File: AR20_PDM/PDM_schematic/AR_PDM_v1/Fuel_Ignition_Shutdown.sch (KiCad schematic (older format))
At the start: 18 parts, among them K1 DIPxx-1Cxx-51x, K2 DIPxx-1Cxx-51x, Q18 N_FET, Q8 N_FET, Q9 N_FET, U2 INA233, U3 INA233

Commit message: Alpha version DONE! - Gerber files generated
- Tweeked
- checked and re cheked
- added all missing components
- Created a really nice silkscreen
- Ready To Test
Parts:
- K1, K2: footprint AR_PDM_v1:Relay -> AR_PDM_v1:Relay_wo_silkscreen
- renumbered C_bypass1 to C44, C_bypass2 to C45, D5 to D30, D6 to D31, Q18 to Q16, Q8 to Q17, Q9 to Q18, R_Shunt1 to R94, R_s13 to R95, R1 to R96, R_Shunt2 to R97, R2 to R98, U2 to U29, U3 to U30

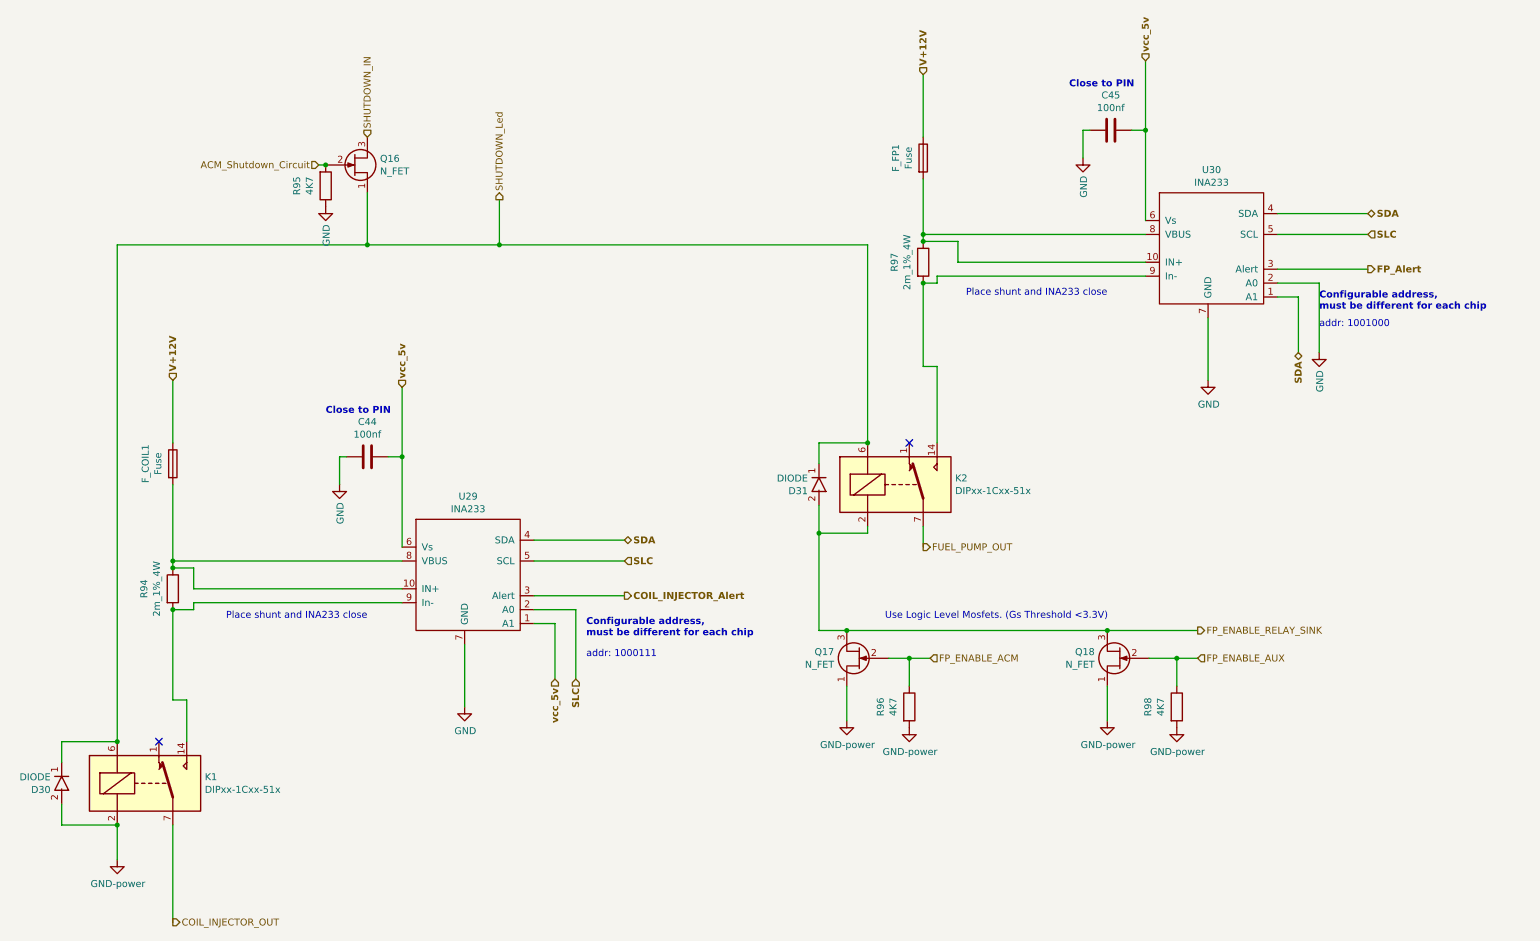
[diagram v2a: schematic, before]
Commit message: Fixed wrong resistors, mos sense. Gerber files updated
- removed all R_is_protection resistors on each mosfet line
- added one R_is_protection resistors to mos_sense_all
ps, mux N-fets, does not need overvoltage protection. 60 volt tolerant.
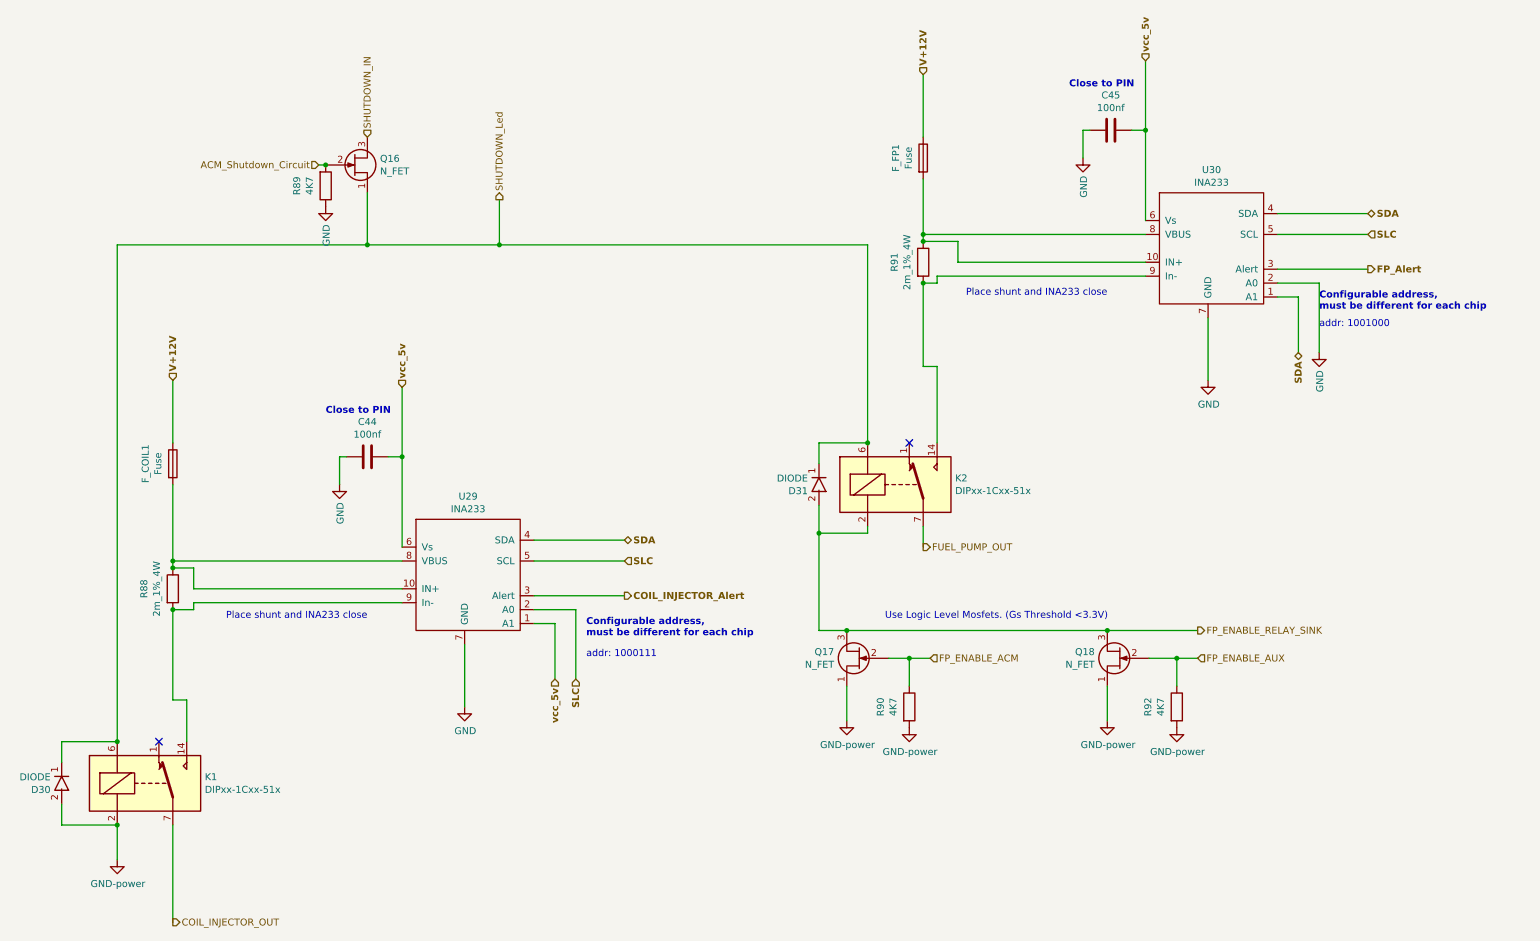
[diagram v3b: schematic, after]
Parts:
- renumbered R94 to R88, R95 to R89, R96 to R90, R97 to R91, R98 to R92
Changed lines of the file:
@@
 P 9175 5550
 AR Path="/5DA89415/5DDB5A5B" Ref="R?"  Part="1"
-AR Path="/5DA8920B/5DDB5A5B" Ref="R98"  Part="1"
-F 0 "R98" V 8968 5550 50  0000 C CNN
+AR Path="/5DA8920B/5DDB5A5B" Ref="R92"  Part="1"
+F 0 "R92" V 8968 5550 50  0000 C CNN
 F 1 "4K7" V 9059 5550 50  0000 C CNN
 F 2 "Resistor_SMD:R_0603_1608Metric" V 9105 5550 50  0001 C CNN
@@
 P 7250 5550
 AR Path="/5DA89415/5DDC298C" Ref="R?"  Part="1"
-AR Path="/5DA8920B/5DDC298C" Ref="R96"  Part="1"
-F 0 "R96" V 7043 5550 50  0000 C CNN
+AR Path="/5DA8920B/5DDC298C" Ref="R90"  Part="1"
+F 0 "R90" V 7043 5550 50  0000 C CNN
 F 1 "4K7" V 7134 5550 50  0000 C CNN
 F 2 "Resistor_SMD:R_0603_1608Metric" V 7180 5550 50  0001 C CNN
@@
 AR Path="/5E0FDCCC/5E1ED477" Ref="R?"  Part="1"
 AR Path="/5E10174B/5E1ED477" Ref="R?"  Part="1"
-AR Path="/5DA8920B/5E1ED477" Ref="R94"  Part="1"
-F 0 "R94" V 1743 4700 50  0000 C CNN
+AR Path="/5DA8920B/5E1ED477" Ref="R88"  Part="1"
+F 0 "R88" V 1743 4700 50  0000 C CNN
 F 1 "2m_1%_4W" V 1834 4700 50  0000 C CNN
 F 2 "Resistor_SMD:R_2512_6332Metric" V 1880 4700 50  0001 C CNN
@@
 AR Path="/5E0FDCCC/5E20008B" Ref="R?"  Part="1"
 AR Path="/5E10174B/5E20008B" Ref="R?"  Part="1"
-AR Path="/5DA8920B/5E20008B" Ref="R97"  Part="1"
-F 0 "R97" V 7143 2350 50  0000 C CNN
+AR Path="/5DA8920B/5E20008B" Ref="R91"  Part="1"
+F 0 "R91" V 7143 2350 50  0000 C CNN
 F 1 "2m_1%_4W" V 7234 2350 50  0000 C CNN
 F 2 "Resistor_SMD:R_2512_6332Metric" V 7280 2350 50  0001 C CNN
@@
 P 3050 1800
 AR Path="/5DA89415/5E265800" Ref="R?"  Part="1"
-AR Path="/5DA8920B/5E265800" Ref="R95"  Part="1"
+AR Path="/5DA8920B/5E265800" Ref="R89"  Part="1"
 AR Path="/5E2546F2/5E265800" Ref="R?"  Part="1"
 AR Path="/5E0FDCCC/5E265800" Ref="R?"  Part="1"
-F 0 "R95" V 2843 1800 50  0000 C CNN
+F 0 "R89" V 2843 1800 50  0000 C CNN
 F 1 "4K7" V 2934 1800 50  0000 C CNN
 F 2 "Resistor_SMD:R_0603_1608Metric" V 2980 1800 50  0001 C CNN

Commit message: Major redesign. schematics completed, PCB work in progress
-TODO : A proper changelog file. Where all changes will apear 
- Redesigned schematics to accommodate errors in the improvement list
- More detail in ALPHA improvement list
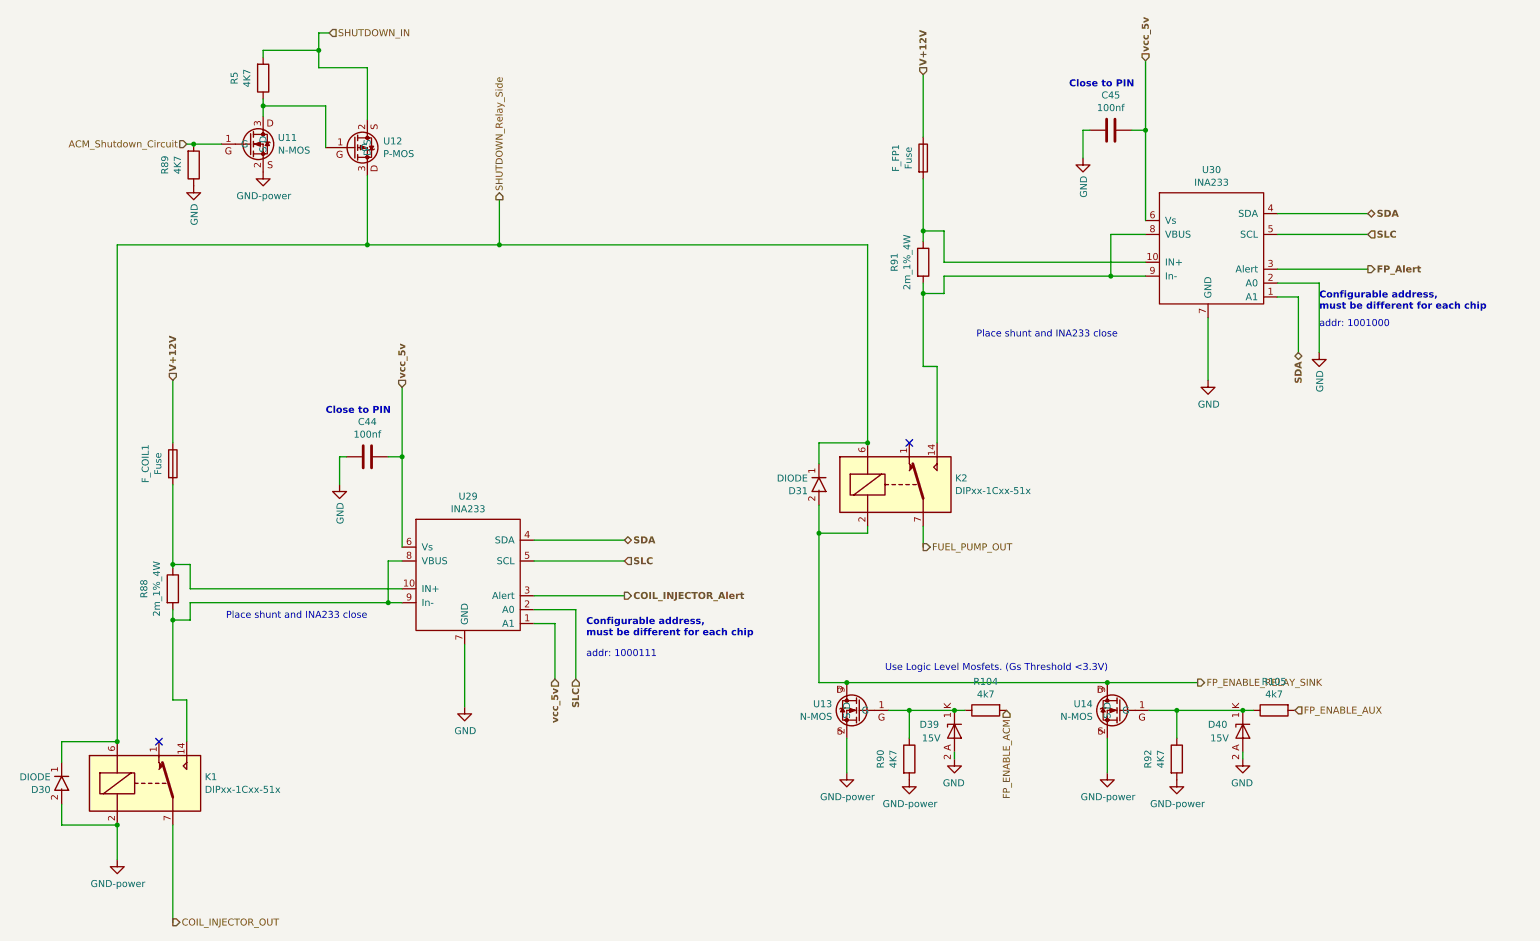
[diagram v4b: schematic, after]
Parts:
- removed Q16, Q17, Q18: N_FET, Package_TO_SOT_SMD:SOT-23, symbol Device:Q_NJFET_DGS
- added D39, D40: 15V, AR_PDM_v1:Diode-BZX585-C15,115, symbol AR20_PDM_v1-rescue:D_Input_protect_zener
- added R104, R105: 4k7, Resistor_SMD:R_0603_1608Metric, symbol AR20_PDM_v1-rescue:R-Device
- added R5: 4K7, Resistor_SMD:R_0603_1608Metric, symbol AR20_PDM_v1-rescue:R-Device
- added U11, U13, U14: N-MOS, AR_PDM_v1:N-MOS-DMN6140L-13, symbol AR20_PDM_v1-rescue:N-MOS-DMN6140L-13
- added U12: P-MOS, AR_PDM_v1:P-MOS-BSS83PH6327XTSA1, symbol AR20_PDM_v1-rescue:P-MOS-BSS83PH6327XTSA1
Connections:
- net ACM_Shutdown_Circuit: now also U11.1 (G)
- net FP_ENABLE_ACM: now also R104.2; no longer R90.1
- net FP_ENABLE_AUX: now also R105.2; no longer R92.1
- net FP_ENABLE_RELAY_SINK: now also U13.3 (D), U14.3 (D)
- net GND: now also D39.2 (A), D40.2 (A), U11.2 (S), U13.2 (S), U14.2 (S)
- net SHUTDOWN_IN: now also R5.2, U12.2 (S)
- net at F_FP1.2, R91.1, U30.10 (IN+): no longer U30.8 (VBUS)
- net at F_COIL1.2, R88.1, U29.10 (IN+): no longer U29.8 (VBUS)
- net at K1.14, R88.2, U29.9 (In-): now also U29.8 (VBUS)
- net at K2.14, R91.2, U30.9 (In-): now also U30.8 (VBUS)
- net SHUTDOWN_Led renamed SHUTDOWN_Relay_Side
- net SHUTDOWN_Relay_Side: now also U12.3 (D)
- new net: D40.1 (K), R105.1, R92.1, U14.1 (G)
- new net: D39.1 (K), R104.1, R90.1, U13.1 (G)
- new net: R5.1, U11.3 (D), U12.1 (G)
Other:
- moved on the sheet: R89, R90, R92

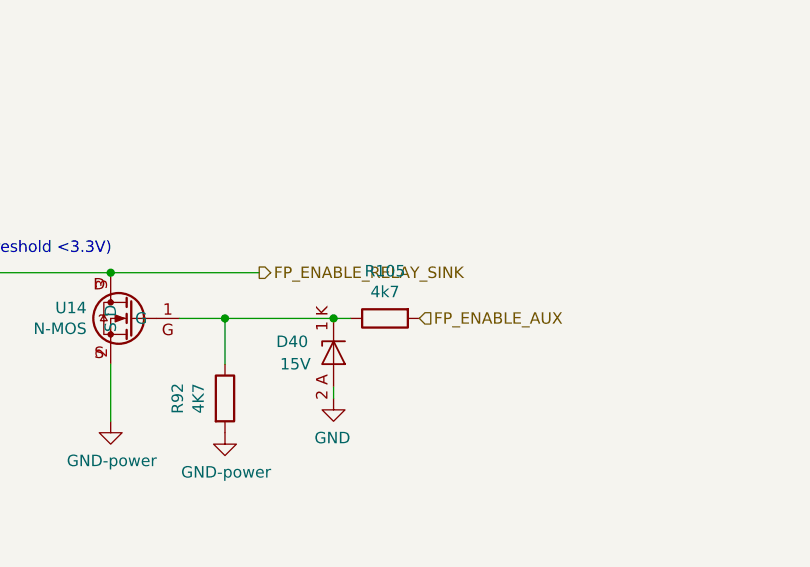
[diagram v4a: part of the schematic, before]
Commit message: All components in place - PCB work in progress
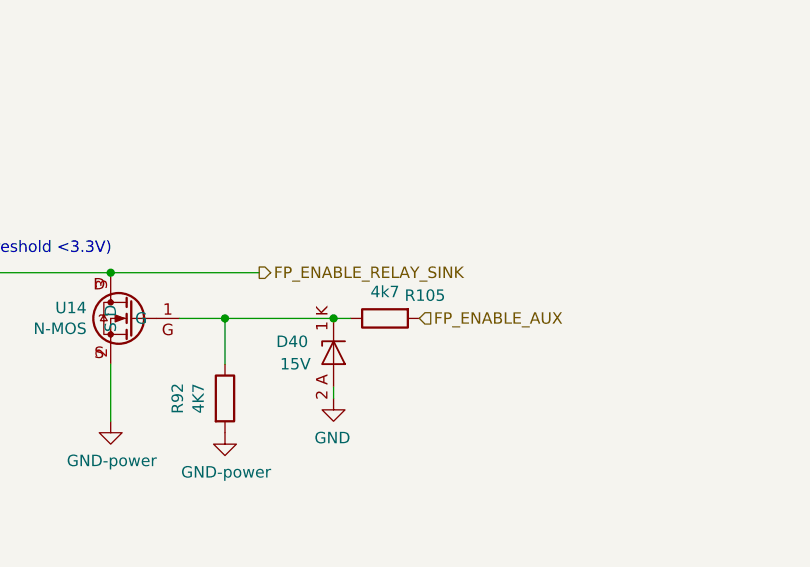
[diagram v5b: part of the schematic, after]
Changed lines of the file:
@@
 $Descr A4 11693 8268
 encoding utf-8
-Sheet 11 14
+Sheet 10 14
 Title ""
 Date ""
@@
 AR Path="/5E683DA7/5E71847A" Ref="R?"  Part="1"
 AR Path="/5DA8920B/5E71847A" Ref="R105"  Part="1"
-F 0 "R105" V 9668 5575 50  0000 C CNN
+F 0 "R105" V 9775 5400 50  0000 C CNN
 F 1 "4k7" V 9759 5575 50  0000 C CNN
 F 2 "Resistor_SMD:R_0603_1608Metric" V 9805 5575 50  0001 C CNN
